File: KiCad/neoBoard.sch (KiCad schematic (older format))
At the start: 74 parts, among them J1 SW, J10 CONN_01X04_Straight, J11 CONN_01X04_Straight, J12 CONN_01X04_Straight, J13 CONN_01X04_Straight, J2 μUSB, J3 BATT, J6 CONN_01X12_Straight, J7 CONN_02X12_Straight, J8 CONN_01X04_Straight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

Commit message: Board
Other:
- note added: "NeoBoard"
- note removed: "Neo Air Shield"
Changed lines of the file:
@@
 LIBS:contrib
 LIBS:valves
-LIBS:placa-cache
-EELAYER 25 0
+EELAYER 26 0
 EELAYER END
 $Descr A4 11693 8268
@@
 Comment4 ""
 $EndDescr
-Text Notes 7050 6800 0    138  ~ 28
-Neo Air Shield
-Text Notes 7050 7000 0    79   ~ 0
+Text Notes 7000 7000 0    236  ~ 47
+NeoBoard
+Text Notes 7050 7300 0    79   ~ 0
 Alvaro Ferrán\n
 Text Notes 800  2100 0    100  ~ 0

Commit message: Change PCA9670 to PCA9685
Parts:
- removed U8: PCA9670, alvaroferran:TSSOP-16, symbol PCA9670
- added U8: PCA9685, alvaroferran:TSSOP-28, symbol PCA9685
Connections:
- wire segments 238 -> 241
- no-connect marks 28 -> 36
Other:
- moved on the sheet: C18, JP1, JP2, JP3, R18, R19, R20

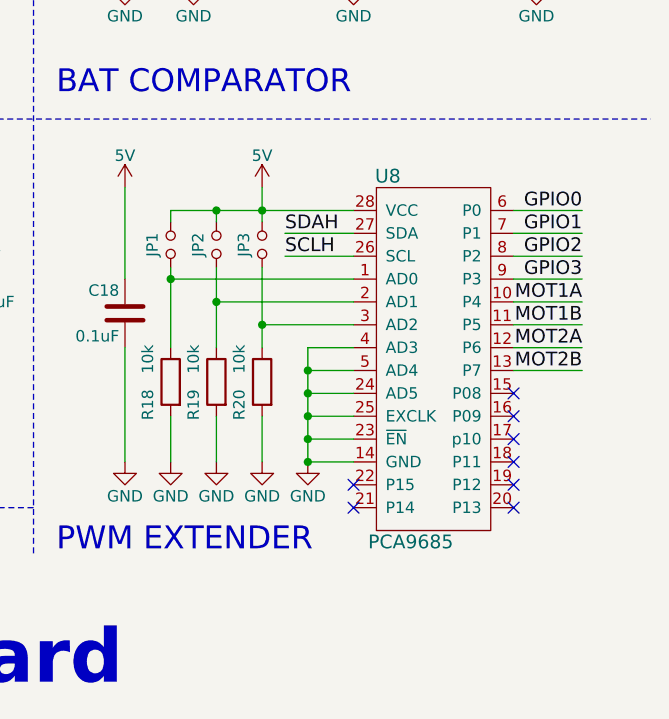
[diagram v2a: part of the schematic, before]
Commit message: Change PCA9670 to PCA9685
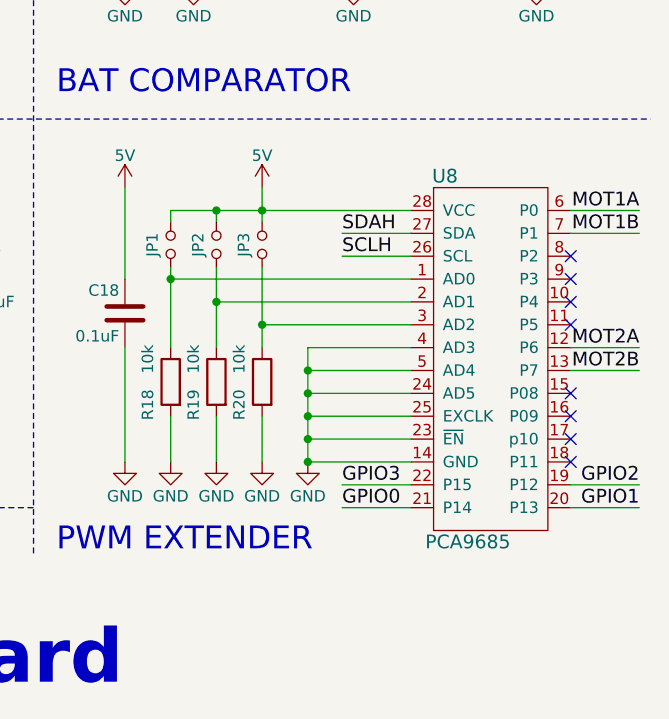
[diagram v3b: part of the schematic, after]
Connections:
- net GPIO0: now also U8.21 (P14); no longer U8.6 (P0)
- net GPIO1: now also U8.20 (P13); no longer U8.7 (P1)
- net GPIO2: now also U8.19 (P12); no longer U8.8 (P2)
- net GPIO3: now also U8.22 (P15); no longer U8.9 (P3)
- net MOT1A: now also U8.6 (P0); no longer U8.10 (P4)
- net MOT1B: now also U8.7 (P1); no longer U8.11 (P5)
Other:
- moved on the sheet: U8
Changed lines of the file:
@@
-EESchema Schematic File Version 2
+EESchema Schematic File Version 3
 LIBS:alvaroferran
 LIBS:power
@@
 LIBS:contrib
 LIBS:valves
+LIBS:neoBoard-cache
 EELAYER 26 0
 EELAYER END
@@
 Text Label 6300 3450 0    60   ~ 0
 SCL
-Text Label 9500 5000 0    60   ~ 0
+Text Label 9750 5000 0    60   ~ 0
 SDAH
-Text Label 9500 5100 0    60   ~ 0
+Text Label 9750 5100 0    60   ~ 0
 SCLH
-Text Label 10800 5300 2    60   ~ 0
+Text Label 11050 4900 2    60   ~ 0
 MOT1A
-Text Label 10800 5400 2    60   ~ 0
+Text Label 11050 5000 2    60   ~ 0
 MOT1B
-Text Label 10800 5500 2    60   ~ 0
+Text Label 11050 5500 2    60   ~ 0
 MOT2A
-Text Label 10800 5600 2    60   ~ 0
+Text Label 11050 5600 2    60   ~ 0
 MOT2B
 Text Notes 8500 6400 0    100  ~ 0
 PWM EXTENDER
-Text Label 10800 4900 2    60   ~ 0
-GPIO0
-Text Label 10800 5000 2    60   ~ 0
-GPIO1
-Text Label 10800 5100 2    60   ~ 0
-GPIO2
-Text Label 10800 5200 2    60   ~ 0
-GPIO3
 $Comp
 L GNDA #PWR032
@@
 L PCA9685 U8
 U 1 1 59C52E90
-P 10200 5300
-F 0 "U8" H 9950 5850 60  0000 C CNN
-F 1 "PCA9685" H 10050 4250 60  0000 C CNN
-F 2 "alvaroferran:TSSOP-28" H 10200 5300 60  0001 C CNN
-F 3 "" H 10200 5300 60  0001 C CNN
-	1    10200 5300
-	1    0    0    -1
-$EndComp
-NoConn ~ 9800 6100
-NoConn ~ 9800 6200
-NoConn ~ 10500 6200
-NoConn ~ 10500 6100
-NoConn ~ 10500 6000
-NoConn ~ 10500 5900
-NoConn ~ 10500 5800
-NoConn ~ 10500 5700
+P 10450 5300
+F 0 "U8" H 10200 5850 60  0000 C CNN
+F 1 "PCA9685" H 10300 4250 60  0000 C CNN
+F 2 "alvaroferran:TSSOP-28" H 10450 5300 60  0001 C CNN
+F 3 "" H 10450 5300 60  0001 C CNN
+	1    10450 5300
+	1    0    0    -1
+$EndComp
+NoConn ~ 10750 6000
+NoConn ~ 10750 5900
+NoConn ~ 10750 5800
+NoConn ~ 10750 5700
 Connection ~ 9400 5400
 Wire Wire Line
-	9800 5400 9400 5400
+	9400 5400 10050 5400
 Connection ~ 9200 5300
 Wire Wire Line
-	9200 5300 9800 5300
+	9200 5300 10050 5300
 Wire Wire Line
 	9000 5150 9000 5500
@@
 Connection ~ 9600 5900
 Wire Wire Line
-	9600 6000 9800 6000
-Wire Wire Line
-	9600 5900 9800 5900
+	9600 6000 10050 6000
+Wire Wire Line
+	9600 5900 10050 5900
 Connection ~ 9600 5800
 Wire Wire Line
-	9600 5800 9800 5800
+	9600 5800 10050 5800
 Connection ~ 9600 5700
 Wire Wire Line
-	9800 5700 9600 5700
+	9600 5700 10050 5700
 Connection ~ 9600 5600
 Wire Wire Line
-	9600 5600 9800 5600
+	9600 5600 10050 5600
 Wire Wire Line
 	9600 5500 9600 6000
 Wire Wire Line
-	9800 5500 9600 5500
+	9600 5500 10050 5500
 Wire Wire Line
 	9400 4800 9400 4950
@@
 Connection ~ 9000 5200
 Wire Wire Line
-	9800 5200 9000 5200
-Wire Wire Line
-	9800 5000 9500 5000
+	9000 5200 10050 5200
+Wire Wire Line
+	10050 5000 9750 5000
 Wire Notes Line
 	8900 600  8900 2200
@@
 	600  4500 11100 4500
 Wire Wire Line
-	9000 4900 9800 4900
+	9000 4900 10050 4900
 Wire Wire Line
 	8800 5500 8800 6000
@@
 	9200 5150 9200 5500
 Wire Wire Line
-	10800 5600 10500 5600
-Wire Wire Line
-	10800 5500 10500 5500
-Wire Wire Line
-	10800 5400 10500 5400
-Wire Wire Line
-	10800 5300 10500 5300
-Wire Wire Line
-	10800 5200 10500 5200
-Wire Wire Line
-	10800 5100 10500 5100
-Wire Wire Line
-	10800 5000 10500 5000
-Wire Wire Line
-	10800 4900 10500 4900
-Wire Wire Line
-	9500 5100 9800 5100
+	11050 5600 10750 5600
+Wire Wire Line
+	11050 5500 10750 5500
+Wire Wire Line
+	9750 5100 10050 5100
 Wire Wire Line
 	6500 3250 6600 3250
@@
 	3300 1300 3300 1200
 Connection ~ 4400 3700
+Wire Wire Line
+	9750 6100 10050 6100
+Wire Wire Line
+	9750 6200 10050 6200
+Text Label 9750 6100 0    60   ~ 0
+GPIO3
+Text Label 9750 6200 0    60   ~ 0
+GPIO0
+Wire Wire Line
+	11050 6100 10750 6100
+Wire Wire Line
+	11050 6200 10750 6200
+Text Label 11050 6200 2    60   ~ 0
+GPIO1
+Text Label 11050 6100 2    60   ~ 0
+GPIO2
+NoConn ~ 10750 5100
+NoConn ~ 10750 5200
+Wire Wire Line
+	11050 5000 10750 5000
+Wire Wire Line
+	11050 4900 10750 4900
+NoConn ~ 10750 5400
+NoConn ~ 10750 5300
 $EndSCHEMATC

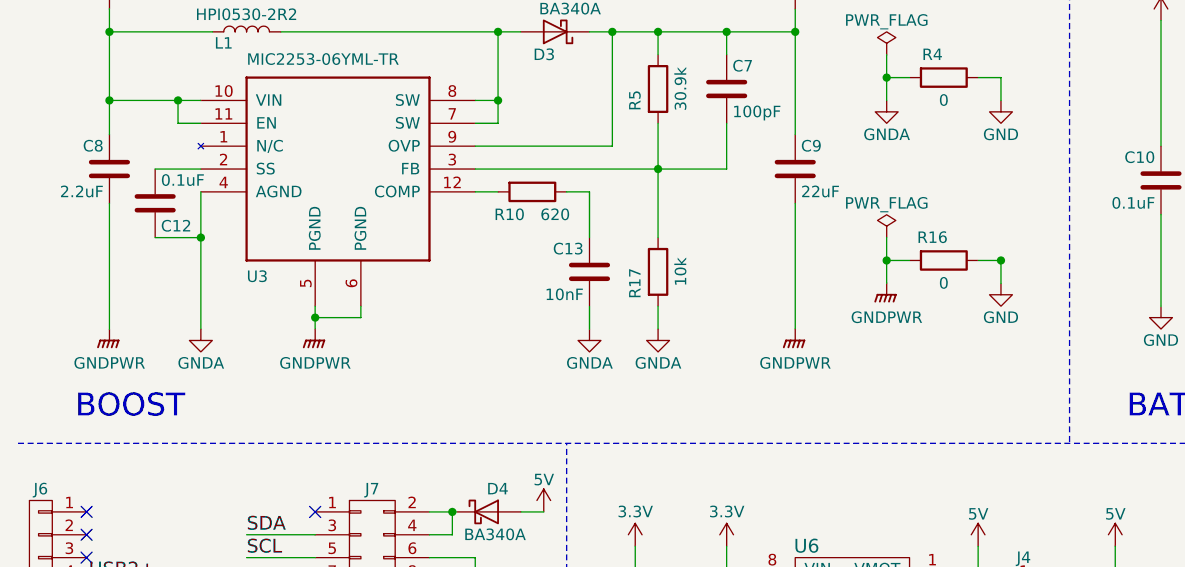
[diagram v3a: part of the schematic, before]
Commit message: Boost circuit re-routed
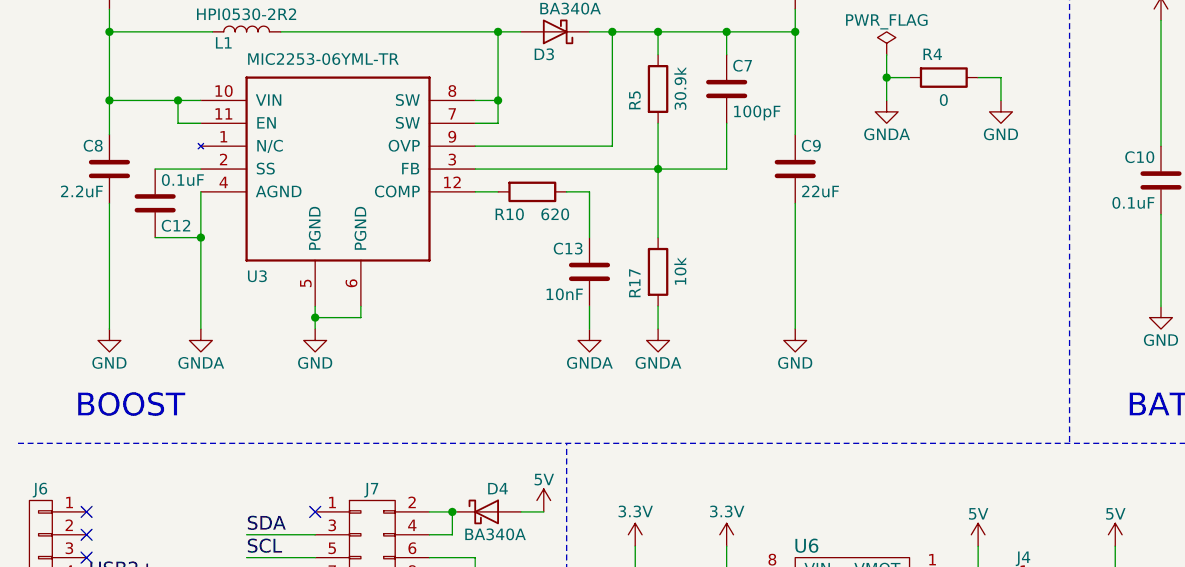
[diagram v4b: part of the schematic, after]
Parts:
- removed R16: 0, Resistors_SMD:R_0603, symbol R0603
- C9: footprint Capacitors_SMD:C_0603 -> Capacitors_SMD:C_0805
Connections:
- net GNDPWR is gone; now on net GND: C8.2, C9.2, U3.5 (PGND), U3.6 (PGND)
